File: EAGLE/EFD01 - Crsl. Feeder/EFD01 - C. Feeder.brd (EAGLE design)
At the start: 160 x 100 mm, 35 parts, among them J1 MOD TOOL, J2 SPI, J3 MOT, J4 FTDI, Q1 BSS138, Q2 16MHz, U1 SP3485, U2 TCST1030, U3 ATMEGA238, U4 DRV8825

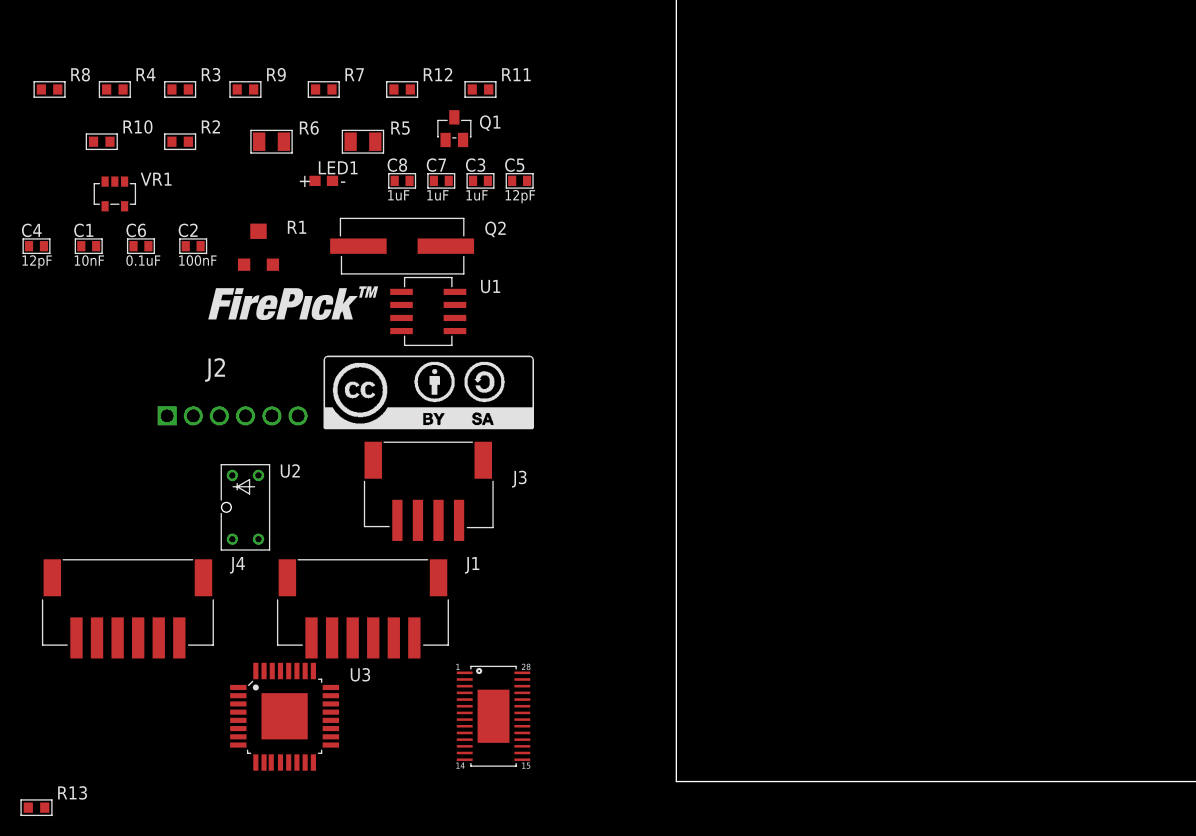
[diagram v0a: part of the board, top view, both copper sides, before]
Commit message: Preliminary placement and routing done for EFD01. Preliminary placement done for EMC03. All schematics are ready for review (A0 for ECAM03 needs to be defined, also SS for EFD01, ECAM03, etc.)
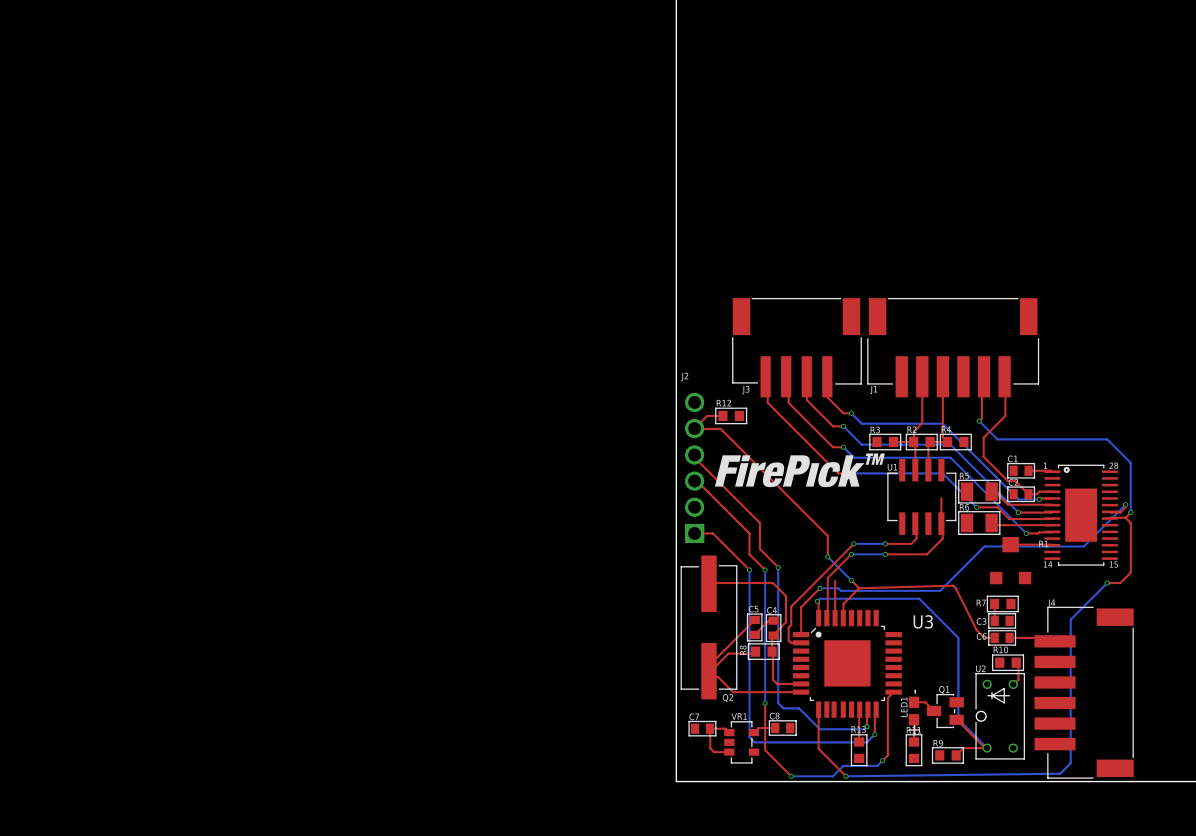
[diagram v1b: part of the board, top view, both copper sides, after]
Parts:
- moved R10 101.7 mm to (32.3, 11.6), turned to 180 degrees
- moved R9 94.1 mm to (26.4, 2.54), turned to 180 degrees
- moved C1 93.3 mm to (33.5, 30.2)
- moved C6 92.0 mm to (31.7, 14.0), turned to 180 degrees
- moved J4 90.3 mm to (36.8, 8.64), turned to 270 degrees
- moved R4 88.7 mm to (27.2, 33.0), turned to 180 degrees
- moved R8 88.4 mm to (8.51, 12.6), turned to 180 degrees
- moved C2 84.1 mm to (33.5, 27.9), turned to 180 degrees
- moved R7 82.9 mm to (31.8, 17.3)
- moved VR1 81.0 mm to (6.35, 3.81), turned to 90 degrees
- moved C4 80.7 mm to (9.46, 14.9), turned to 270 degrees
- moved R13 80.2 mm to (17.8, 3.05), turned to 90 degrees
- moved R1 79.2 mm to (32.5, 21.6)
- moved LOGO1 78.4 mm to (43.9, 29.0), flipped to the bottom
- moved R6 78.2 mm to (29.5, 25.1)
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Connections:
- removed net !ENBL: U3.9, U4.21
- net !ENABLE: now also U3.9, U4.21
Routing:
- net !ENABLE: track 0.00 -> 85.1 mm, vias 0 -> 4
- net SCK: track 0.00 -> 49.4 mm, vias 0 -> 4
- net RESET: track 0.00 -> 46.6 mm, vias 0 -> 2
- net STEP: track 0.00 -> 40.6 mm, vias 0 -> 2
- net MOSI: track 0.00 -> 39.0 mm, vias 0 -> 2
- net MISO: track 0.00 -> 38.3 mm, vias 0 -> 2
- net O_OUT: track 0.00 -> 36.4 mm, vias 0 -> 1
- net BOUT2: track 0.00 -> 35.0 mm, vias 0 -> 2
- net BOUT1: track 0.00 -> 33.6 mm, vias 0 -> 2
- net AOUT2: track 0.00 -> 30.7 mm, vias 0 -> 2
- net AOUT1: track 0.00 -> 28.6 mm, vias 0 -> 2
- net XTAL2: track 0.00 -> 21.9 mm
- net DTR1: track 0.00 -> 21.2 mm, vias 0 -> 2
- net DI: track 0.00 -> 20.7 mm, vias 0 -> 2
- net XTAL1: track 0.00 -> 19.9 mm
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
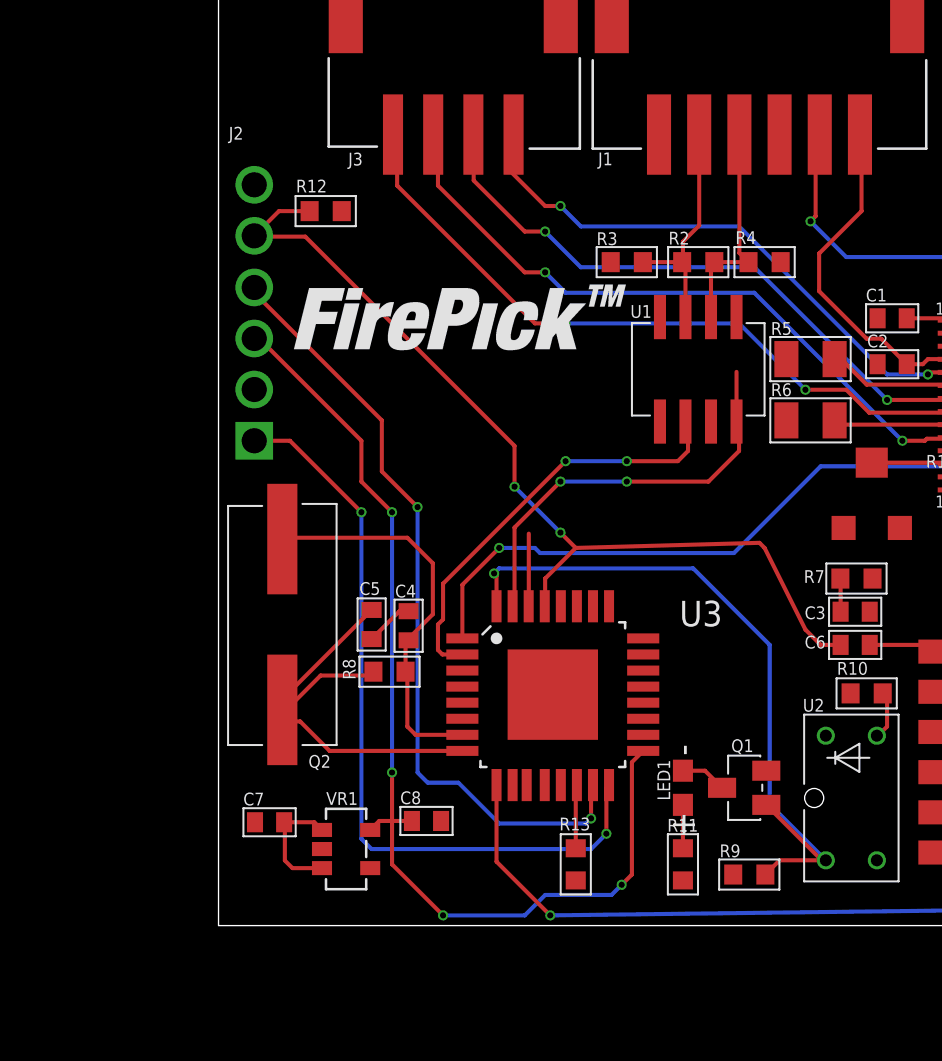
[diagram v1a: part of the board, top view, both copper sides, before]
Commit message: Finalized schematics (minus potential LDO regulator) for all boards. Layout partially done for EFD01
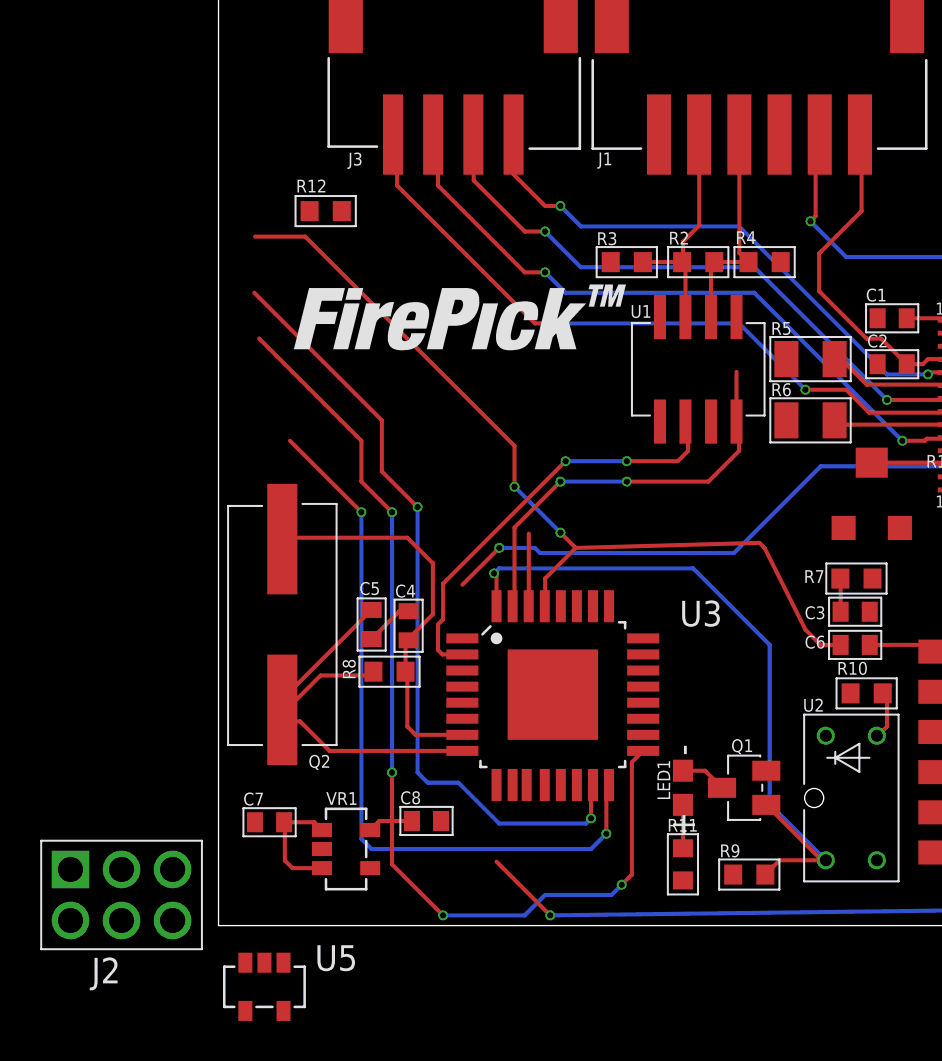
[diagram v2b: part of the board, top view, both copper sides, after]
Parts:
- removed R13: 10K, TinWhiskers:R0603
- added U5: 74LVC, TinWhiskers:SOT-23-5
- J2: device TinWhiskers:CON-HDR-6POS-MALE -> TinWhiskers:CON-HDR-2X3P
- moved J2 29.7 mm to (-4.83, 1.52), turned to 0 degrees
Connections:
- removed net SS: R13.2, U3.14
- new net !ENBL_AVR: U3.11, U5.2
- new net !ENBL_MOD: J1.2, U5.1
- net !ENABLE: now also U5.4; no longer J1.2, U3.9
- net +3V3: now also U5.5
- net +5V: no longer R13.1
- net DIR: now also U3.10
- net GND: now also U5.3
- net STEP: now also U3.9; no longer U3.1
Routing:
- net !ENABLE: track 85.1 -> 81.0 mm
- net RESET: track 46.6 -> 43.2 mm
- net SS: track 3.17 -> 0.00 mm
- net STEP: track 40.6 -> 37.9 mm
- net MISO: track 38.3 -> 36.5 mm

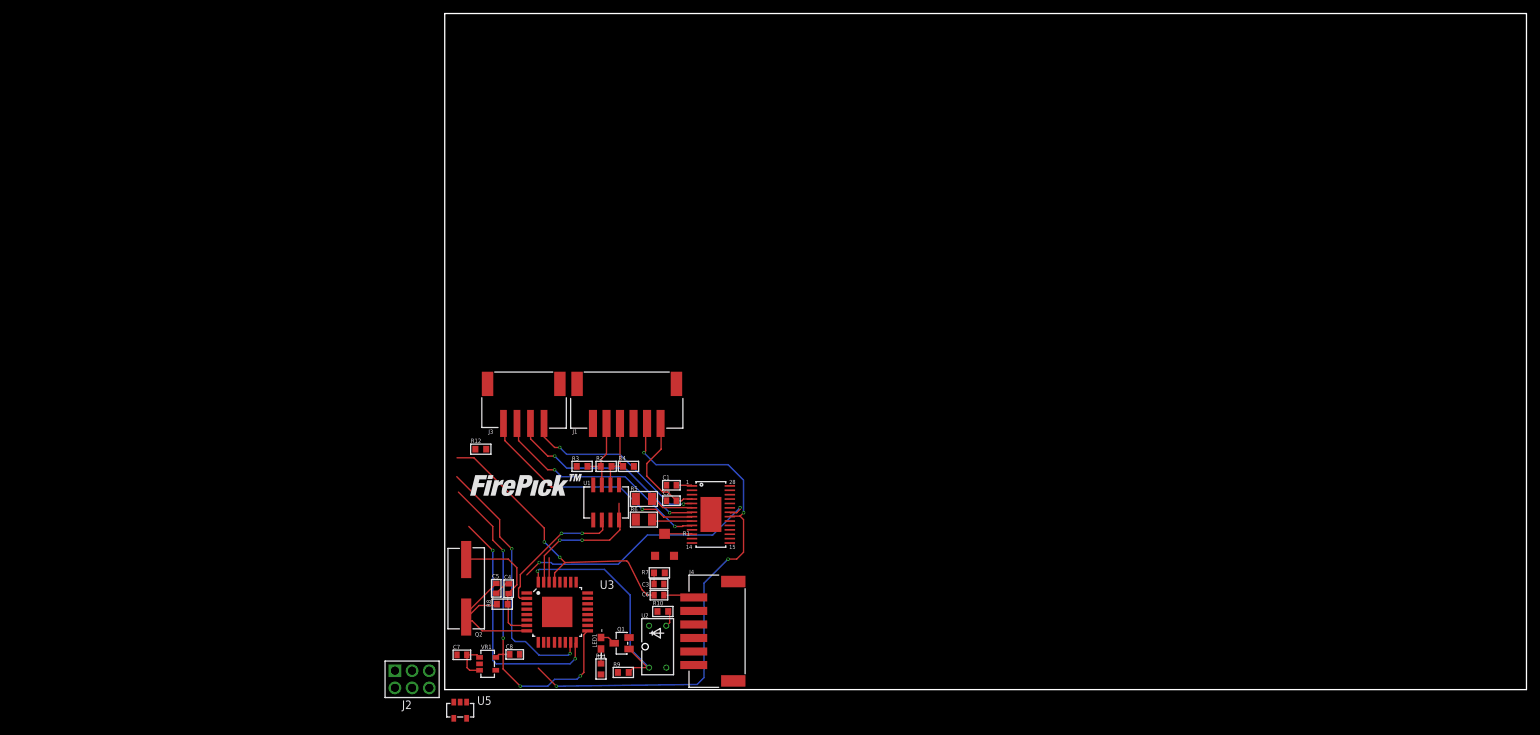
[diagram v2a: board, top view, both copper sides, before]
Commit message: Routed EFD01, ECAM03 boards. Modification needs to be made for hole/keepout in ECAM03. EMC03 X and Y sides routed. Will need to increase some trace widths.
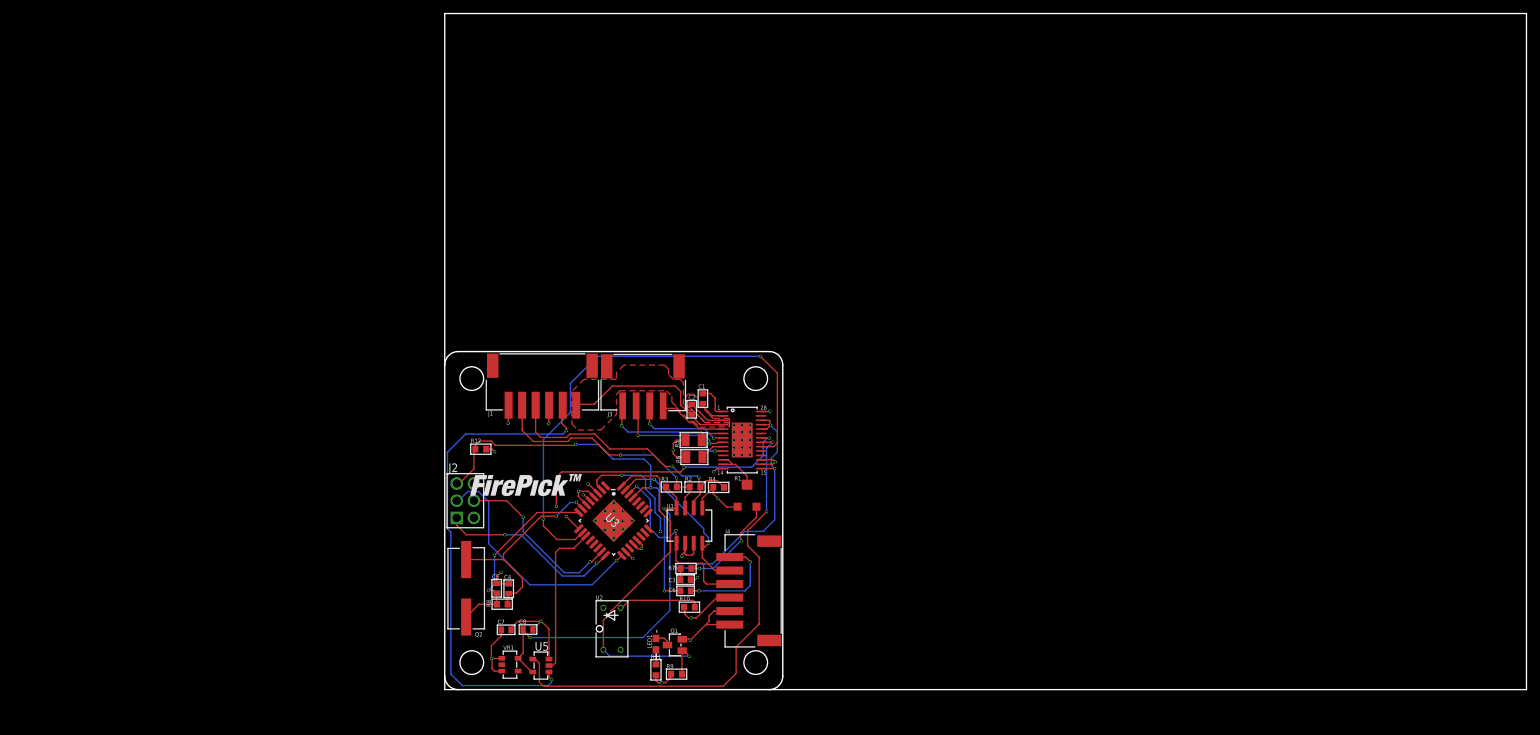
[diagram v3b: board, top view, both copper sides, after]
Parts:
- removed LOGO1: LOGO-CC-BY-SALARGE, FirePick:LOGO-CC-BY-SA
- moved J2 27.6 mm to (3.05, 27.9), turned to 90 degrees
- moved J3 17.8 mm to (29.3, 42.0)
- moved U3 15.9 mm to (25.0, 25.0), turned to 315 degrees
- moved R1 14.2 mm to (44.7, 28.9)
- moved C2 13.9 mm to (36.5, 41.5), turned to 90 degrees
- moved R4 13.7 mm to (40.5, 29.9), turned to 0 degrees
- moved U5 13.6 mm to (14.2, 3.56), turned to 270 degrees
- moved C1 13.6 mm to (38.2, 43.0), turned to 90 degrees
- moved R3 13.6 mm to (33.5, 30.0)
- moved R2 13.5 mm to (37.0, 30.0)
- moved U1 12.8 mm to (36.2, 24.3)
- moved J1 12.8 mm to (14.5, 42.1)
- moved U4 11.9 mm to (44.0, 36.9)
- moved R6 11.9 mm to (36.9, 34.4)
- moved R5 11.4 mm to (36.8, 36.9)
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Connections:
- net N$7 renamed VCP
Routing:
- net DIR: track 0.00 -> 76.0 mm, vias 0 -> 2
- net !ENBL_MOD: track 0.00 -> 73.5 mm, vias 0 -> 2
- net GND: track 2.42 -> 57.7 mm, vias 0 -> 40
- net +3V3: track 2.26 -> 52.7 mm, vias 0 -> 2
- net N$13: track 1.66 -> 42.4 mm, vias 0 -> 3
- net +5V: track 5.97 -> 37.9 mm, vias 0 -> 8
- net A: track 11.1 -> 40.7 mm, vias 0 -> 2
- net RO: track 3.62 -> 28.8 mm, vias 0 -> 2
- net B: track 11.5 -> 36.5 mm, vias 0 -> 2
- net !ENBL_AVR: track 0.00 -> 23.0 mm
- net AOUT1: track 28.6 -> 10.3 mm, vias 2 -> 0
- net O_OUT: track 36.4 -> 54.4 mm
- net RESET: track 43.2 -> 60.4 mm, vias 2 -> 3
- net AOUT2: track 30.7 -> 14.5 mm
- net BOUT2: track 35.0 -> 19.5 mm
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- added copper zone on layer 1, net +24V
- added copper zone on layer 15, net +5V
- added copper zone on layer 2, net GND
- added copper zone on layer 1, net VCP
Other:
- outline, holes or cut-outs redrawn

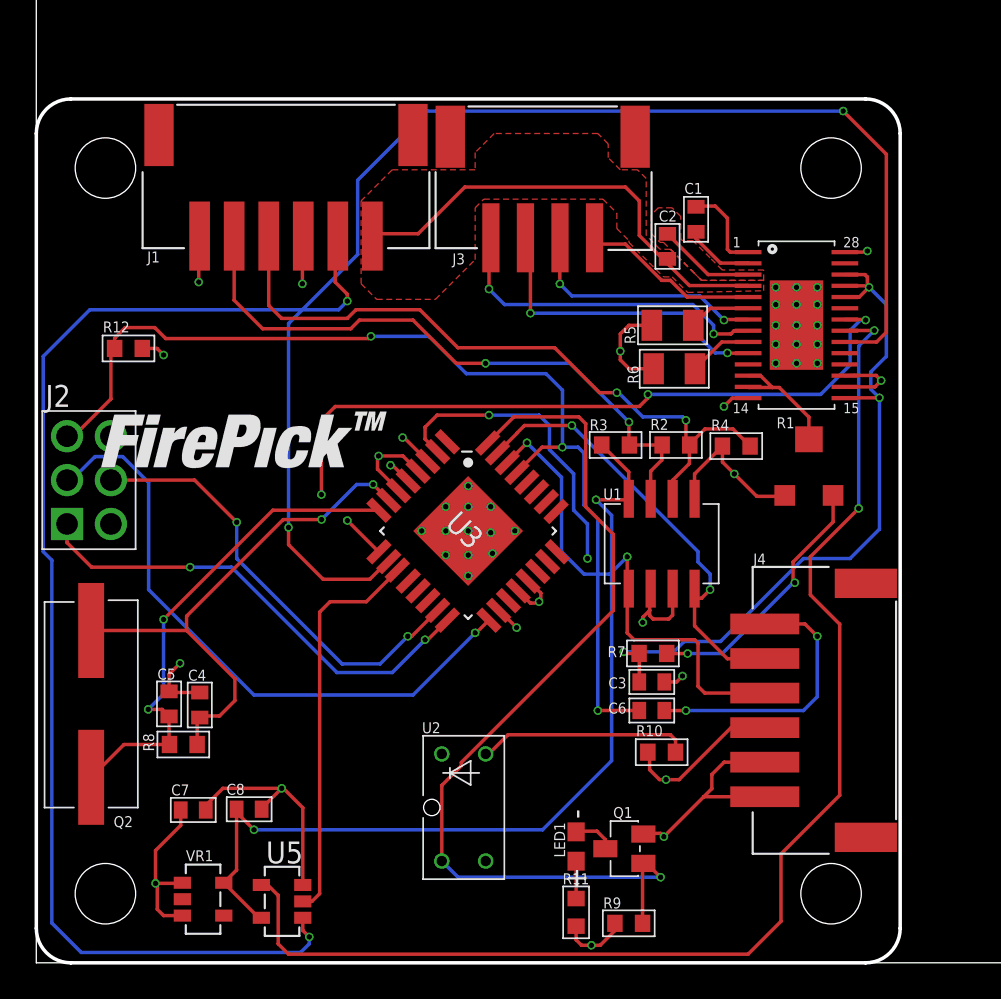
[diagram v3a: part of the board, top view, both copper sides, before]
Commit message: Completed boards. Please look at airwires connecting thermal pads to GND vias. They shouldn't be present due to the vias.
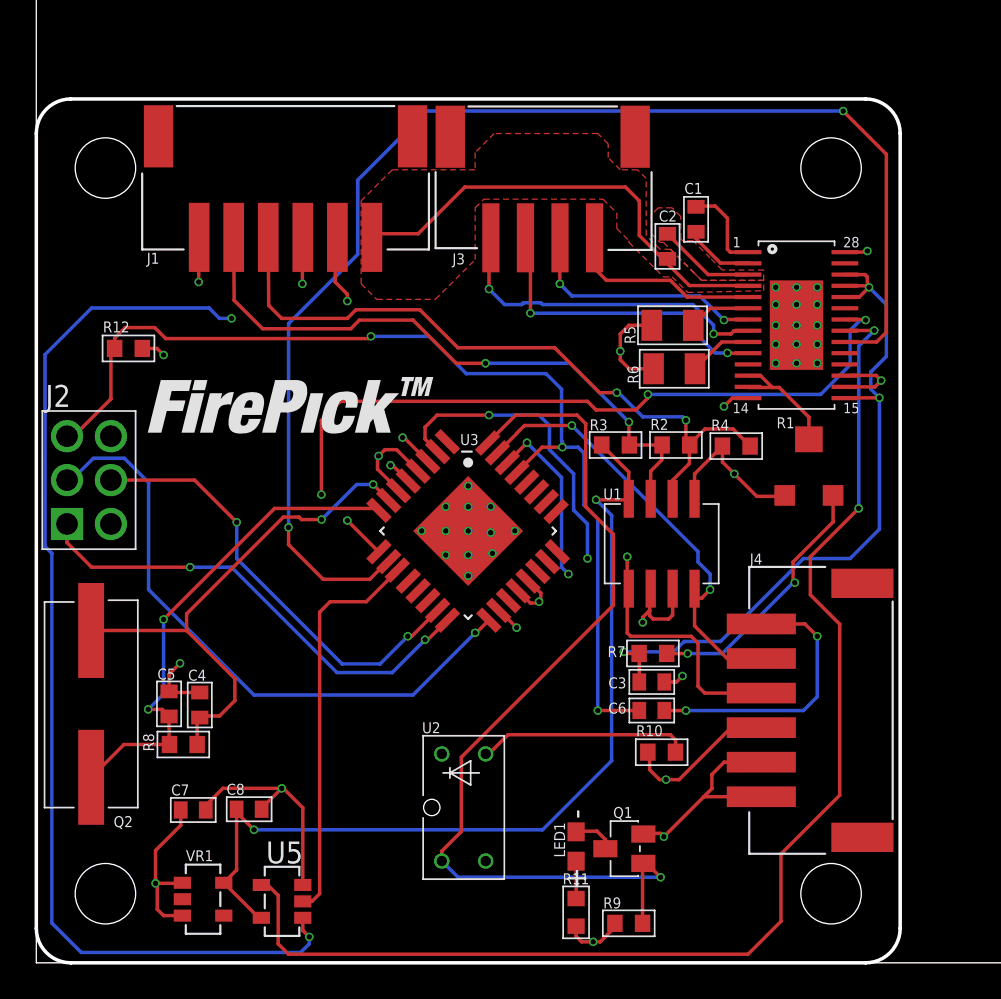
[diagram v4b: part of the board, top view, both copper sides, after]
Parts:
- moved LOGO2 3.36 mm to (6.26, 28.9)
- moved J4 0.20 mm to (42.0, 14.6)
- moved J1 0.08 mm to (14.4, 42.0)
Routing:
- net AOUT1: track 10.3 -> 11.4 mm
- net !ENBL_MOD: track 73.5 -> 73.9 mm, vias 2 -> 3
- net RO: track 28.8 -> 29.2 mm, vias 2 -> 3
